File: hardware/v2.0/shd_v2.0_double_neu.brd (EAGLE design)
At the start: 69 x 43.8 mm, 24 parts

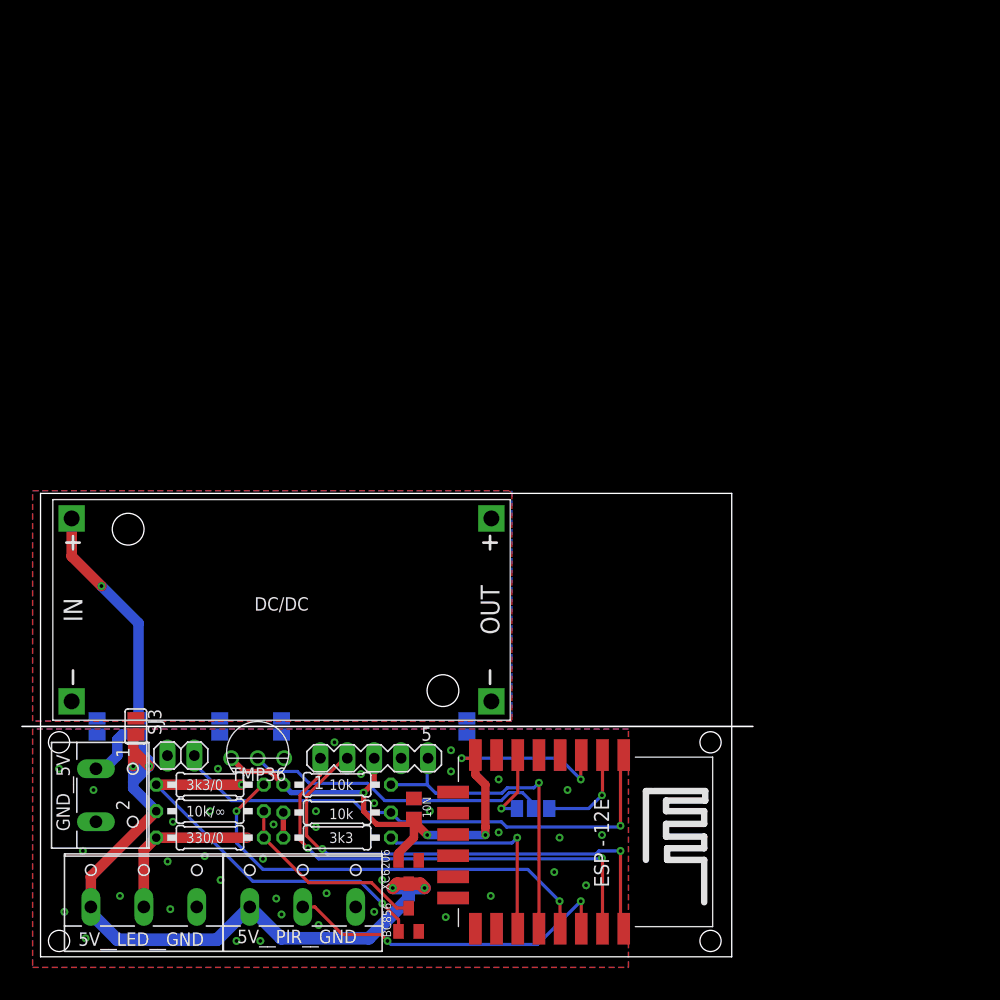
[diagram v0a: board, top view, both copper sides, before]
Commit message: adds hardware v2.0 and software support for dht22 sensor
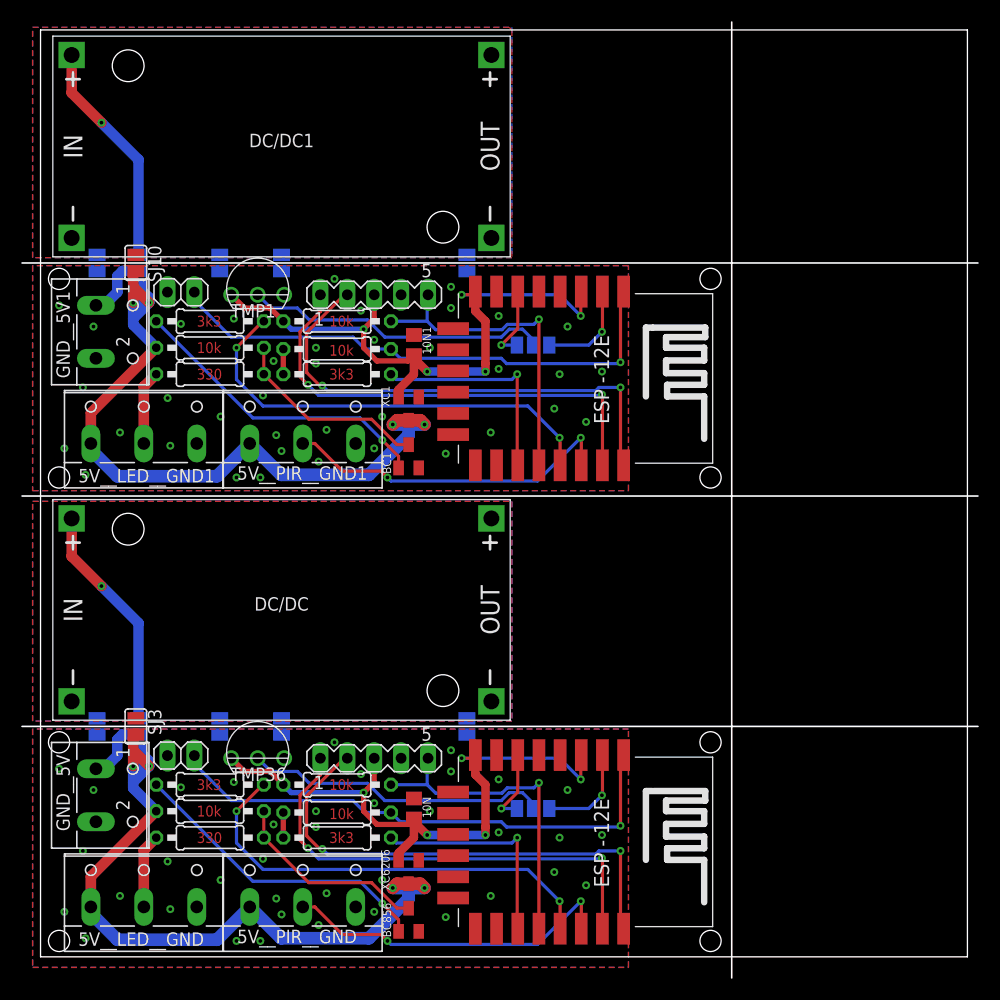
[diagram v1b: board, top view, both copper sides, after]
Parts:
- added 10N1: (no value), eagle-ltspice:C0805
- added 5V__LED__GND1, 5V__PIR__GND1: (no value), con-wago-500:W237-103
- added BC1: (no value), transistor:SOT23-BEC
- added DC/DC1: DC-DC-STEP-DOWN-LM2596, diy-modules:DC-DC-STEP-DOWN-LM2596
- added GND__5V1: (no value), con-wago-500:W237-102
- added JP2: (no value), pinhead:1X02
- added PROG_INTERFACE1: (no value), con-lstb:MA05-1
- added R_GPIO1, R_LED_B1: 3k3, eagle-ltspice:0207/10
- added R_LED_C2, R_PROG1, R_RST1: 10k, eagle-ltspice:0207/10
- added R_LED_C3: 330, eagle-ltspice:0207/10
- added SJ10, SJ11, SJ12, SJ13, SJ14: (no value), jumper:SJ
- added SJ8, SJ9: (no value), jumper:SJ_2
- added TMP1: TMP36, tmp36:TO-92
- added U2: (no value), esp8266modules:ESP12E-SMD
- added XC1: (no value), Voltage Regulator:SOT23
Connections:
- new net GND1: 10N1.2, 5V__LED__GND1.3, 5V__PIR__GND1.3, BC1.E, GND__5V1.2, JP2.1, PROG_INTERFACE1.4, SJ11.1, SJ12.1, SJ13.1, SJ14.1, TMP1.3, U2.GND, U2.GPIO15, XC1.1
- new net GND_STEP_DOWN1: DC/DC1.IN-, DC/DC1.OUT-, SJ11.2, SJ12.2, SJ13.2, SJ14.2
- new net GPIO1: PROG_INTERFACE1.5, R_PROG1.1, U2.GPIO0
- new net LED_DATA_3.1: R_LED_B1.2, U2.GPIO4
- new net LED_DATA_3.3_R1: BC1.B, R_LED_B1.1
- new net LED_DATA_5.1: BC1.C, R_LED_C2.1, R_LED_C3.2
- new net LED_DATA_OUT1: 5V__LED__GND1.2, R_LED_C3.1
- new net N$1: R_GPIO1.2, U2.GPIO2
- new net PIR1: 5V__PIR__GND1.2, U2.GPIO5
- new net RST1: JP2.2, R_RST1.1, U2.RESET
- new net RX1: PROG_INTERFACE1.1, U2.RXD0
- new net TMP_ANA1: SJ8.1, U2.ADC
- new net TMP_DATA1: SJ8.3, U2.GPIO12
- new net TX1: PROG_INTERFACE1.2, U2.TXD0
- new net VCC_5.1: 5V__LED__GND1.1, 5V__PIR__GND1.1, R_LED_C2.2, SJ10.2, SJ9.1, XC1.3
- new net VCC_STEP_DOWN1: DC/DC1.OUT+, SJ10.1
- new net VDD_3.1: 10N1.1, PROG_INTERFACE1.3, R_GPIO1.1, R_PROG1.2, R_RST1.2, TMP1.1, U2.CH_PD, U2.VCC, XC1.2
- new net V_IN1: GND__5V1.1, SJ9.2
- new net V_IN_2: DC/DC1.IN+, SJ9.3
- new net V_TMP1: SJ8.2, TMP1.2
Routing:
- net VCC_5.1: track 0.00 -> 72.2 mm, vias 0 -> 4
- net VDD_3.1: track 0.00 -> 63.0 mm, vias 0 -> 5
- net RST1: track 0.00 -> 50.3 mm, vias 0 -> 1
- net TX1: track 0.00 -> 47.0 mm, vias 0 -> 2
- net RX1: track 0.00 -> 44.5 mm, vias 0 -> 2
- net LED_DATA_3.1: track 0.00 -> 42.0 mm, vias 0 -> 2
- net PIR1: track 0.00 -> 32.0 mm, vias 0 -> 2
- net GPIO1: track 0.00 -> 31.1 mm, vias 0 -> 1
- net LED_DATA_3.3_R1: track 0.00 -> 29.3 mm, vias 0 -> 1
- net V_TMP1: track 0.00 -> 28.9 mm
- net V_IN_2: track 0.00 -> 21.5 mm, vias 0 -> 1
- net N$1: track 0.00 -> 21.0 mm, vias 0 -> 1
- net LED_DATA_5.1: track 0.00 -> 18.9 mm
- net TMP_ANA1: track 0.00 -> 9.31 mm, vias 0 -> 1
- net LED_DATA_OUT: track 15.6 -> 7.02 mm, vias 1 -> 0
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- added copper zone on layer 1, net GND1
- added copper zone on layer 16, net GND1
- added copper zone on layer 16, net GND_STEP_DOWN1
- added copper zone on layer 1, net VCC_STEP_DOWN1
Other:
- board size 69 x 43.8 mm -> 90.2 x 90.2 mm
- board text added: "330"
- board text removed: "10k/∞"
- board text removed: "330/0"
- board text removed: "3k3/0"
